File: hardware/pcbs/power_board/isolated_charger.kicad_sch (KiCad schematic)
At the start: 11 parts, among them J5 USB_A, U1 VRB1205S-6WR3, U2 LTV-247, U3 NCP380

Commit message: power_board: initial outline
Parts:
- U1: Shop https://www.digikey.com/en/products/detail/mean-well-usa-in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 -> https://eu.mouser.com/ProductDetail/MEAN-WELL/SPBW06F-05?qs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
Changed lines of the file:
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@@
 			)
 		)
-		(property "Shop" "https://www.digikey.com/en/products/detail/mean-well-usa-inc/SPBW06F-05/7707011 or https://www.digikey.com/en/products/detail/mornsun-america-llc/VRB1205S-6WR3/16348304?s=N4IgTCBcDaIGoCUBCBGMAGArAZQLQDYB1BAZhAF0BfIA"
+		(property "Shop" "https://eu.mouser.com/ProductDetail/MEAN-WELL/SPBW06F-05?qs=5aG0NVq1C4xl9jmeoQl1uw%3D%3D"
 			(at 95.25 96.52 0)
 			(effects

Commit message: audio_board, power_board: update shop and part links
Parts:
- C2: Part (none) -> C 10μF 16V 0805
- C3, C4: Part (none) -> C 1μF 16V 0805
- R4: Part (none) -> R 4.7kΩ 125mW 5% 0805
- R5: Part (none) -> R 36kΩ 125mW 1% 0805
- R6: Part (none) -> R 100Ω 125mW 5% 0805
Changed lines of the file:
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@@
+			)
+		)
+		(property "Part" "C 10μF 16V 0805"
+			(at 120.65 102.87 0)
+			(effects
+				(font
+					(size 1.27 1.27)
+				)
+				(hide yes)
 			)
 		)
@@
 			)
 		)
+		(property "Part" "R 4.7kΩ 125mW 5% 0805"
+			(at 152.4 58.42 0)
+			(effects
+				(font
+					(size 1.27 1.27)
+				)
+				(hide yes)
+			)
+		)
 		(pin "1"
 		)
@@
 			)
 		)
+		(property "Part" "C 1μF 16V 0805"
+			(at 201.93 102.87 0)
+			(effects
+				(font
+					(size 1.27 1.27)
+				)
+				(hide yes)
+			)
+		)
 		(pin "1"
 		)
@@
 			)
 		)
+		(property "Part" "R 36kΩ 125mW 1% 0805"
+			(at 181.61 106.68 0)
+			(effects
+				(font
+					(size 1.27 1.27)
+				)
+				(hide yes)
+			)
+		)
 		(pin "1"
 		)
@@
 		)
 		(property "LCSC" "C28323"
+			(at 132.08 102.87 0)
+			(effects
+				(font
+					(size 1.27 1.27)
+				)
+				(hide yes)
+			)
+		)
+		(property "Part" "C 1μF 16V 0805"
 			(at 132.08 102.87 0)
 			(effects
@@
 			(at 241.3 95.25 0)
 			(effects
+				(font
+					(size 1.27 1.27)
+				)
+				(hide yes)
+			)
+		)
+		(property "Part" "R 100Ω 125mW 5% 0805"
+			(at 241.3 95.25 0)
+			(effects

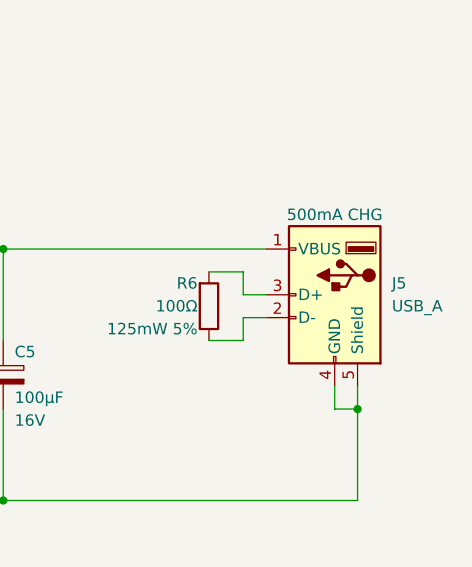
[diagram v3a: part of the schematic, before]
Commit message: power_board: final-ish shape
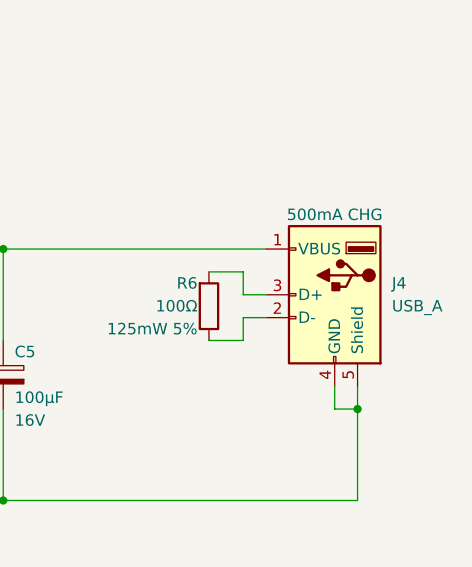
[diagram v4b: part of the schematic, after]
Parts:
- renumbered J5 to J4
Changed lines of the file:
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@@
 		(on_board yes)
 		(dnp no)
-		(property "Reference" "J5"
+		(property "Reference" "J4"
 			(at 261.62 92.71 0)
 			(effects
@@
 			(project "power_board"
 				(path "/4b166175-80a4-48c6-994d-6e62a6160b87/2e2b9578-5dbd-4b2d-88fb-256ac9c8dd75/32f9baea-32bc-4a84-b83a-18c67cc6248e"
+					(reference "J4")
+					(unit 1)
+				)
+				(path "/4b166175-80a4-48c6-994d-6e62a6160b87/2e2b9578-5dbd-4b2d-88fb-256ac9c8dd75/5f362cd5-d351-4250-994a-9f336837035c"
 					(reference "J5")
 					(unit 1)
 				)
-				(path "/4b166175-80a4-48c6-994d-6e62a6160b87/2e2b9578-5dbd-4b2d-88fb-256ac9c8dd75/5f362cd5-d351-4250-994a-9f336837035c"
+				(path "/4b166175-80a4-48c6-994d-6e62a6160b87/2e2b9578-5dbd-4b2d-88fb-256ac9c8dd75/6373063e-1125-40d9-b0ec-3e2cb2886aea"
 					(reference "J6")
 					(unit 1)
 				)
-				(path "/4b166175-80a4-48c6-994d-6e62a6160b87/2e2b9578-5dbd-4b2d-88fb-256ac9c8dd75/6373063e-1125-40d9-b0ec-3e2cb2886aea"
+				(path "/4b166175-80a4-48c6-994d-6e62a6160b87/2e2b9578-5dbd-4b2d-88fb-256ac9c8dd75/bdb69c9c-123a-4faa-b5c1-7130aac5ebc2"
 					(reference "J7")
-					(unit 1)
-				)
-				(path "/4b166175-80a4-48c6-994d-6e62a6160b87/2e2b9578-5dbd-4b2d-88fb-256ac9c8dd75/bdb69c9c-123a-4faa-b5c1-7130aac5ebc2"
-					(reference "J8")
 					(unit 1)
 				)
@@
 		(dnp no)
 		(fields_autoplaced yes)
-		(property "Reference" "#PWR017"
+		(property "Reference" "#PWR011"
 			(at 179.07 72.39 0)
 			(effects
@@
 		(dnp no)
 		(fields_autoplaced yes)
-		(property "Reference" "#PWR016"
+		(property "Reference" "#PWR010"
 			(at 78.74 120.65 0)
 			(effects

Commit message: power_board: final touches
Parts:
- J4: Purpose 500mA CHG -> CHG
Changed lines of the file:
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@@
 			)
 		)
-		(property "Purpose" "500mA CHG"
+		(property "Purpose" "CHG"
 			(at 255.27 85.09 0)
 			(effects

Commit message: boards: update boms again
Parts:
- C5: Part RK1C101M-RBD11 -> CP 100μF 16V P2
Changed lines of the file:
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@@
 			)
 		)
-		(property "Part" "RK1C101M-RBD11"
+		(property "Part" "CP 100μF 16V P2"
 			(at 218.44 102.87 0)
 			(effects

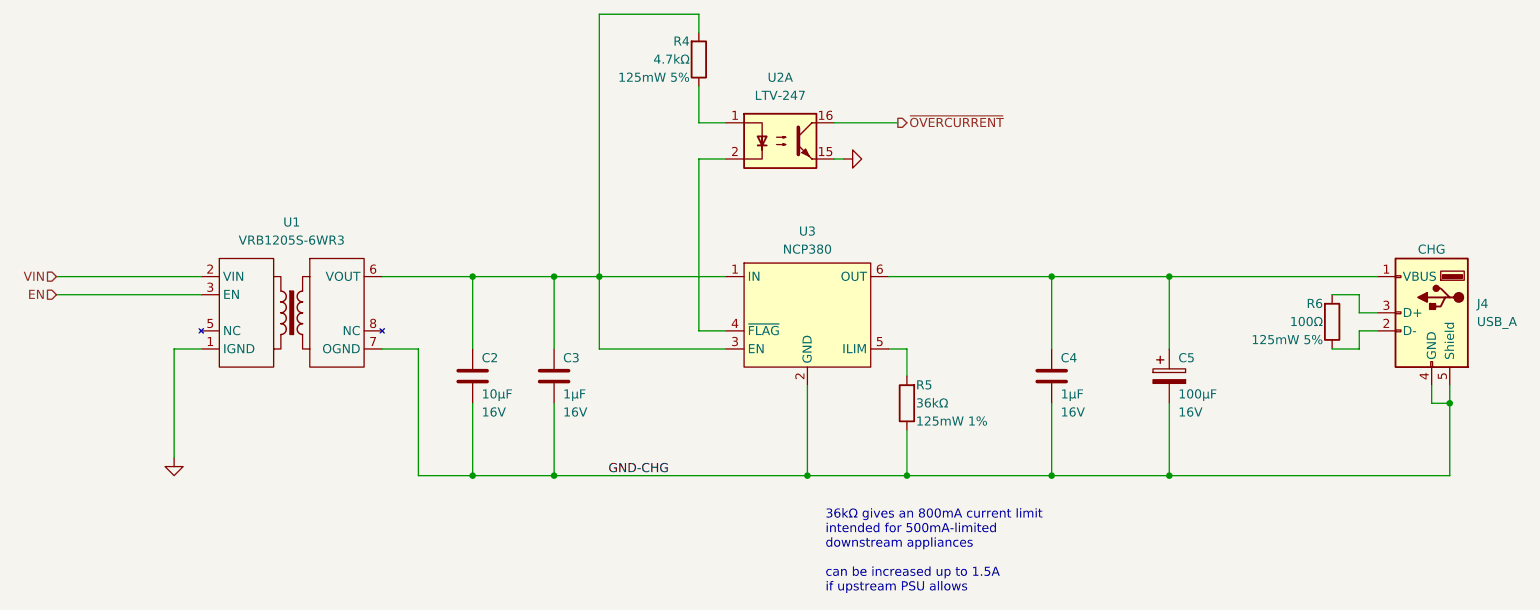
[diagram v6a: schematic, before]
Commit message: power_board: use USB3-A passthrough connector and fix chg EN
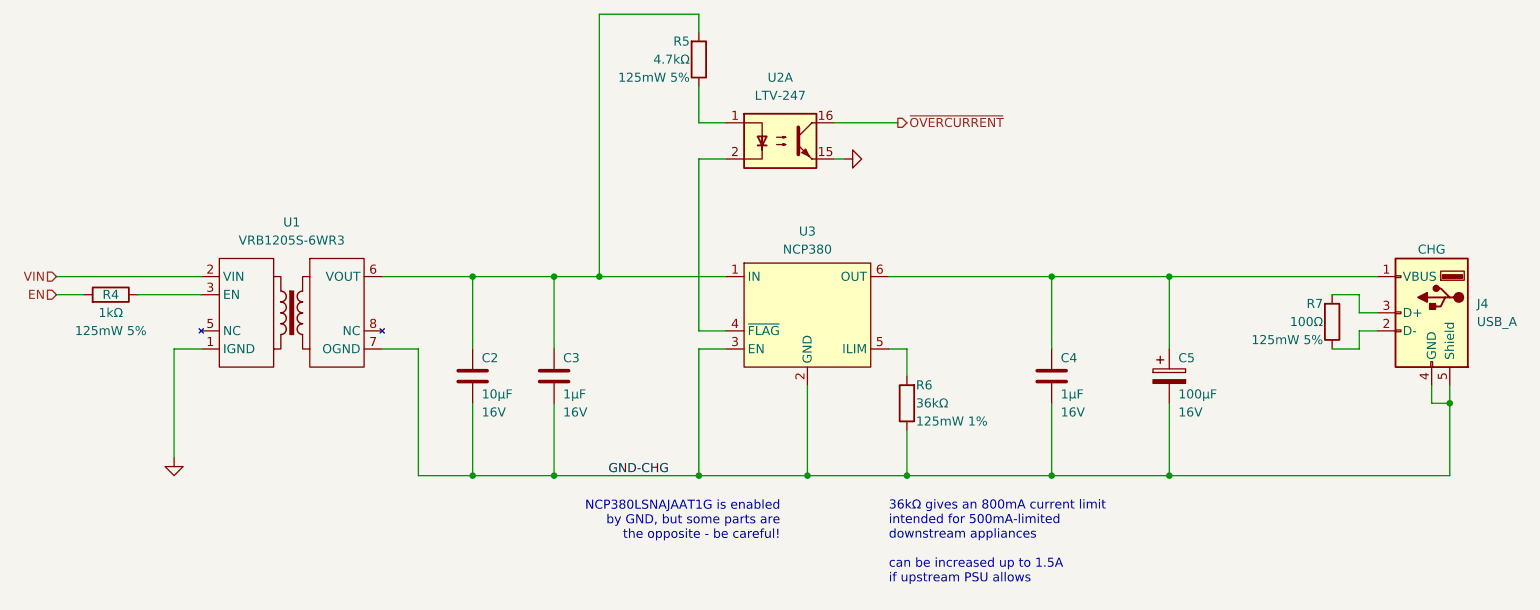
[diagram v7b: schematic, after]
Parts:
- added R4: 1kΩ, Resistor_SMD:R_0805_2012Metric, symbol Device:R
- renumbered R4 to R5, R5 to R6, R6 to R7
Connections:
- net EN: now also R4.2; no longer U1.3 (EN)
- net GND-CHG: now also U3.3 (EN)
- net at C2.1, C3.1, R5.2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: no longer U3.3 (EN)
- new net: R4.1, U1.3 (EN)
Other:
- note added: "NCP380LSNAJAAT1G is enabled by GND, but some parts are the opposite - be careful!"
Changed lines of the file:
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@@
+	)
+	(junction
+		(at 152.4 116.84)
+		(diameter 0)
+		(color 0 0 0 0)
 	)
 	(junction
@@
 	(wire
 		(pts
-			(xy 132.08 116.84) (xy 167.64 116.84)
+			(xy 73.66 91.44) (xy 82.55 91.44)
+		)
+		(stroke
+			(width 0)
+			(type default)
+		)
+	)
+	(wire
+		(pts
+			(xy 132.08 116.84) (xy 152.4 116.84)
 		)
 		(stroke
@@
 	(wire
 		(pts
+			(xy 152.4 116.84) (xy 167.64 116.84)
+		)
+		(stroke
+			(width 0)
+			(type default)
+		)
+	)
+	(wire
+		(pts
 			(xy 181.61 99.06) (xy 179.07 99.06)
 		)
@@
 	(wire
 		(pts
-			(xy 156.21 99.06) (xy 138.43 99.06)
-		)
-		(stroke
-			(width 0)
-			(type default)
-		)
-	)
-	(wire
-		(pts
 			(xy 179.07 88.9) (xy 201.93 88.9)
 		)
@@
 	(wire
 		(pts
+			(xy 156.21 99.06) (xy 152.4 99.06)
+		)
+		(stroke
+			(width 0)
+			(type default)
+		)
+	)
+	(wire
+		(pts
 			(xy 171.45 67.31) (xy 180.34 67.31)
 		)
@@
 	(wire
 		(pts
+			(xy 152.4 99.06) (xy 152.4 116.84)
+		)
+		(stroke
+			(width 0)
+			(type default)
+		)
+	)
+	(wire
+		(pts
 			(xy 245.11 91.44) (xy 245.11 93.98)
 		)
@@
 	(wire
 		(pts
-			(xy 62.23 91.44) (xy 82.55 91.44)
+			(xy 62.23 91.44) (xy 66.04 91.44)
 		)
 		(stroke
@@
 	(wire
 		(pts
-			(xy 138.43 99.06) (xy 138.43 88.9)
-		)
-		(stroke
-			(width 0)
-			(type default)
-		)
-	)
-	(wire
-		(pts
 			(xy 138.43 88.9) (xy 156.21 88.9)
 		)
@@
 			(width 0)
 			(type default)
+		)
+	)
+	(text "NCP380LSNAJAAT1G is enabled\nby GND, but some parts are\nthe opposite - be careful!"
+		(exclude_from_sim no)
+		(at 163.83 123.19 0)
+		(effects
+			(font
+				(size 1.27 1.27)
+			)
+			(justify right)
 		)
 	)
 	(text "36kΩ gives an 800mA current limit\nintended for 500mA-limited\ndownstream appliances\n\ncan be increased up to 1.5A\nif upstream PSU allows"
 		(exclude_from_sim no)
-		(at 170.18 133.35 0)
+		(at 179.07 132.08 0)
 		(effects
 			(font
@@
 	(symbol
 		(lib_id "Device:R")
+		(at 69.85 91.44 270)
+		(mirror x)
+		(unit 1)
+		(exclude_from_sim no)
+		(in_bom yes)
+		(on_board yes)
+		(dnp no)
+		(property "Reference" "R4"
+			(at 69.85 91.44 90)
+			(effects
+				(font
+					(size 1.27 1.27)
+				)
+			)
+		)
+		(property "Value" "1kΩ"
+			(at 69.85 93.98 90)
+			(effects
+				(font
+					(size 1.27 1.27)
+				)
+			)
+		)
+		(property "Footprint" "Resistor_SMD:R_0805_2012Metric"
+			(at 69.85 93.218 90)
+			(effects
+				(font
+					(size 1.27 1.27)
+				)
+				(hide yes)
+			)
+		)
+		(property "Datasheet" "~"
+			(at 69.85 91.44 0)
+			(effects
+				(font
+					(size 1.27 1.27)
+				)
+				(hide yes)
+			)
+		)
+		(property "Description" ""
+			(at 69.85 91.44 0)
+			(effects
+				(font
+					(size 1.27 1.27)
+				)
+				(hide yes)
+			)
+		)
+		(property "Info" "125mW 5%"
+			(at 69.85 96.52 90)
+			(effects
+				(font
+					(size 1.27 1.27)
+				)
+			)
+		)
+		(property "Shop" "https://store.comet.bg/Catalogue/Product/29754/"
+			(at 69.85 91.44 0)
+			(effects
+				(font
+					(size 1.27 1.27)
+				)
+				(hide yes)
+			)
+		)
+		(property "LCSC" ""
+			(at 69.85 91.44 0)
+			(effects
+				(font
+					(size 1.27 1.27)
+				)
+				(hide yes)
+			)
+		)
+		(property "Part" "R 1kΩ 125mW 5% 0805"
+			(at 69.85 91.44 0)
+			(effects
+				(font
+					(size 1.27 1.27)
+				)
+				(hide yes)
+			)
+		)
+		(pin "1"
+		)
+		(pin "2"
+		)
+		(instances
+			(project "power_board"
+				(path "/4b166175-80a4-48c6-994d-6e62a6160b87/2e2b9578-5dbd-4b2d-88fb-256ac9c8dd75/32f9baea-32bc-4a84-b83a-18c67cc6248e"
+					(reference "R4")
+					(unit 1)
+				)
+				(path "/4b166175-80a4-48c6-994d-6e62a6160b87/2e2b9578-5dbd-4b2d-88fb-256ac9c8dd75/5f362cd5-d351-4250-994a-9f336837035c"
+					(reference "R8")
+					(unit 1)
+				)
+				(path "/4b166175-80a4-48c6-994d-6e62a6160b87/2e2b9578-5dbd-4b2d-88fb-256ac9c8dd75/6373063e-1125-40d9-b0ec-3e2cb2886aea"
+					(reference "R12")
+					(unit 1)
+				)
+				(path "/4b166175-80a4-48c6-994d-6e62a6160b87/2e2b9578-5dbd-4b2d-88fb-256ac9c8dd75/bdb69c9c-123a-4faa-b5c1-7130aac5ebc2"
+					(reference "R16")
+					(unit 1)
+				)
+			)
+		)
+	)
+	(symbol
+		(lib_id "Device:R")
 		(at 152.4 58.42 0)
 		(mirror x)
@@
 		(on_board yes)
 		(dnp no)
-		(property "Reference" "R4"
+		(property "Reference" "R5"
 			(at 151.13 55.88 0)
 			(effects
@@
 			(project "power_board"
 				(path "/4b166175-80a4-48c6-994d-6e62a6160b87/2e2b9578-5dbd-4b2d-88fb-256ac9c8dd75/32f9baea-32bc-4a84-b83a-18c67cc6248e"
-					(reference "R4")
+					(reference "R5")
 					(unit 1)
 				)
 				(path "/4b166175-80a4-48c6-994d-6e62a6160b87/2e2b9578-5dbd-4b2d-88fb-256ac9c8dd75/5f362cd5-d351-4250-994a-9f336837035c"
-					(reference "R7")
+					(reference "R9")
 					(unit 1)
 				)
 				(path "/4b166175-80a4-48c6-994d-6e62a6160b87/2e2b9578-5dbd-4b2d-88fb-256ac9c8dd75/6373063e-1125-40d9-b0ec-3e2cb2886aea"
-					(reference "R10")
+					(reference "R13")
 					(unit 1)
 				)
 				(path "/4b166175-80a4-48c6-994d-6e62a6160b87/2e2b9578-5dbd-4b2d-88fb-256ac9c8dd75/bdb69c9c-123a-4faa-b5c1-7130aac5ebc2"
-					(reference "R13")
+					(reference "R17")
 					(unit 1)
 				)
@@
 		(dnp no)
 		(fields_autoplaced yes)
-		(property "Reference" "#PWR011"
+		(property "Reference" "#PWR010"
 			(at 179.07 72.39 0)
 			(effects
@@
 			(project "power_board"
 				(path "/4b166175-80a4-48c6-994d-6e62a6160b87/2e2b9578-5dbd-4b2d-88fb-256ac9c8dd75/32f9baea-32bc-4a84-b83a-18c67cc6248e"
-					(reference "#PWR011")
+					(reference "#PWR010")
 					(unit 1)
 				)
 				(path "/4b166175-80a4-48c6-994d-6e62a6160b87/2e2b9578-5dbd-4b2d-88fb-256ac9c8dd75/5f362cd5-d351-4250-994a-9f336837035c"
-					(reference "#PWR013")
+					(reference "#PWR012")
 					(unit 1)
 				)
 				(path "/4b166175-80a4-48c6-994d-6e62a6160b87/2e2b9578-5dbd-4b2d-88fb-256ac9c8dd75/6373063e-1125-40d9-b0ec-3e2cb2886aea"
-					(reference "#PWR015")
+					(reference "#PWR014")
 					(unit 1)
 				)
 				(path "/4b166175-80a4-48c6-994d-6e62a6160b87/2e2b9578-5dbd-4b2d-88fb-256ac9c8dd75/bdb69c9c-123a-4faa-b5c1-7130aac5ebc2"
-					(reference "#PWR017")
+					(reference "#PWR016")
 					(unit 1)
 				)
@@
 		(on_board yes)
 		(dnp no)
-		(property "Reference" "R5"
+		(property "Reference" "R6"
 			(at 182.88 104.14 0)
 			(effects
@@
 			(project "power_board"
 				(path "/4b166175-80a4-48c6-994d-6e62a6160b87/2e2b9578-5dbd-4b2d-88fb-256ac9c8dd75/32f9baea-32bc-4a84-b83a-18c67cc6248e"
-					(reference "R5")
+					(reference "R6")
 					(unit 1)
 				)
 				(path "/4b166175-80a4-48c6-994d-6e62a6160b87/2e2b9578-5dbd-4b2d-88fb-256ac9c8dd75/5f362cd5-d351-4250-994a-9f336837035c"
-					(reference "R8")
+					(reference "R10")
 					(unit 1)
 				)
 				(path "/4b166175-80a4-48c6-994d-6e62a6160b87/2e2b9578-5dbd-4b2d-88fb-256ac9c8dd75/6373063e-1125-40d9-b0ec-3e2cb2886aea"
-					(reference "R11")
+					(reference "R14")
 					(unit 1)
 				)
 				(path "/4b166175-80a4-48c6-994d-6e62a6160b87/2e2b9578-5dbd-4b2d-88fb-256ac9c8dd75/bdb69c9c-123a-4faa-b5c1-7130aac5ebc2"
-					(reference "R14")
+					(reference "R18")
 					(unit 1)
 				)
@@
 		(on_board yes)
 		(dnp no)
-		(property "Reference" "R6"
+		(property "Reference" "R7"
 			(at 240.03 92.71 0)
 			(effects
@@
 			(project "power_board"
 				(path "/4b166175-80a4-48c6-994d-6e62a6160b87/2e2b9578-5dbd-4b2d-88fb-256ac9c8dd75/32f9baea-32bc-4a84-b83a-18c67cc6248e"
-					(reference "R6")
+					(reference "R7")
 					(unit 1)
 				)
 				(path "/4b166175-80a4-48c6-994d-6e62a6160b87/2e2b9578-5dbd-4b2d-88fb-256ac9c8dd75/5f362cd5-d351-4250-994a-9f336837035c"
-					(reference "R9")
+					(reference "R11")
 					(unit 1)
 				)
 				(path "/4b166175-80a4-48c6-994d-6e62a6160b87/2e2b9578-5dbd-4b2d-88fb-256ac9c8dd75/6373063e-1125-40d9-b0ec-3e2cb2886aea"
-					(reference "R12")
+					(reference "R15")
 					(unit 1)
 				)
 				(path "/4b166175-80a4-48c6-994d-6e62a6160b87/2e2b9578-5dbd-4b2d-88fb-256ac9c8dd75/bdb69c9c-123a-4faa-b5c1-7130aac5ebc2"
-					(reference "R15")
+					(reference "R19")
 					(unit 1)
 				)
@@
 		(dnp no)
 		(fields_autoplaced yes)
-		(property "Reference" "#PWR010"
+		(property "Reference" "#PWR09"
 			(at 78.74 120.65 0)
 			(effects
@@
 			(project "power_board"
 				(path "/4b166175-80a4-48c6-994d-6e62a6160b87/2e2b9578-5dbd-4b2d-88fb-256ac9c8dd75/32f9baea-32bc-4a84-b83a-18c67cc6248e"
-					(reference "#PWR010")
+					(reference "#PWR09")
 					(unit 1)
 				)
 				(path "/4b166175-80a4-48c6-994d-6e62a6160b87/2e2b9578-5dbd-4b2d-88fb-256ac9c8dd75/5f362cd5-d351-4250-994a-9f336837035c"
-					(reference "#PWR012")
+					(reference "#PWR011")
 					(unit 1)
 				)
 				(path "/4b166175-80a4-48c6-994d-6e62a6160b87/2e2b9578-5dbd-4b2d-88fb-256ac9c8dd75/6373063e-1125-40d9-b0ec-3e2cb2886aea"
-					(reference "#PWR014")
+					(reference "#PWR013")
 					(unit 1)
 				)
 				(path "/4b166175-80a4-48c6-994d-6e62a6160b87/2e2b9578-5dbd-4b2d-88fb-256ac9c8dd75/bdb69c9c-123a-4faa-b5c1-7130aac5ebc2"
-					(reference "#PWR016")
-					(unit 1)
-				)
+					(reference "#PWR015")
+					(unit 1)
+				)
